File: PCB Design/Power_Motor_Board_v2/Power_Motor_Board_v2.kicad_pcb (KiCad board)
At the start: 2 copper layers, 98.2 x 100 mm, 38 parts, among them IC1 DRV8251ADDAR, IC3 DRV8251ADDAR, IC4 AP63205WU-7, J1 691137710002, J2 691137710002, J2A1 SSW-119-01-T-D, J3 691137710002, J4 Conn_01x06, J5 Conn_01x02_Socket

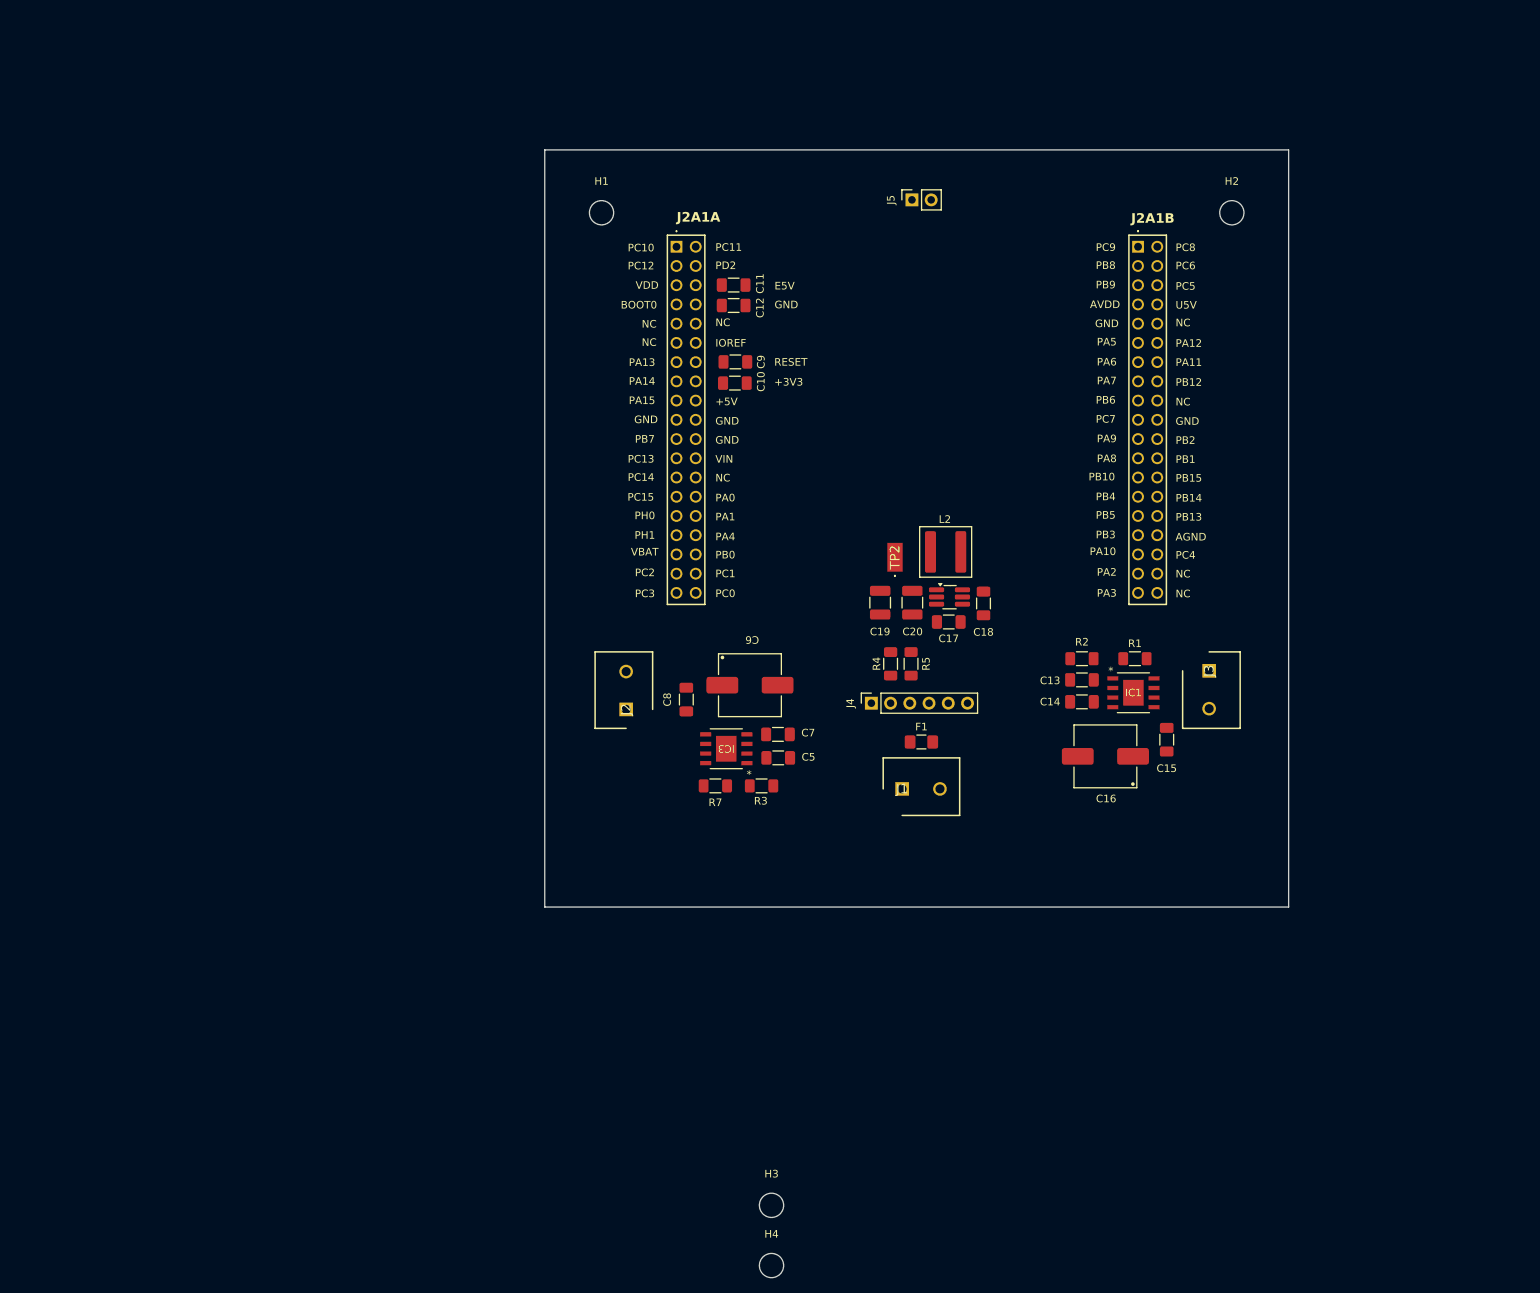
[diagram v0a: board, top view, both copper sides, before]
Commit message: Continued board layout and mesurements as well as edited BOM
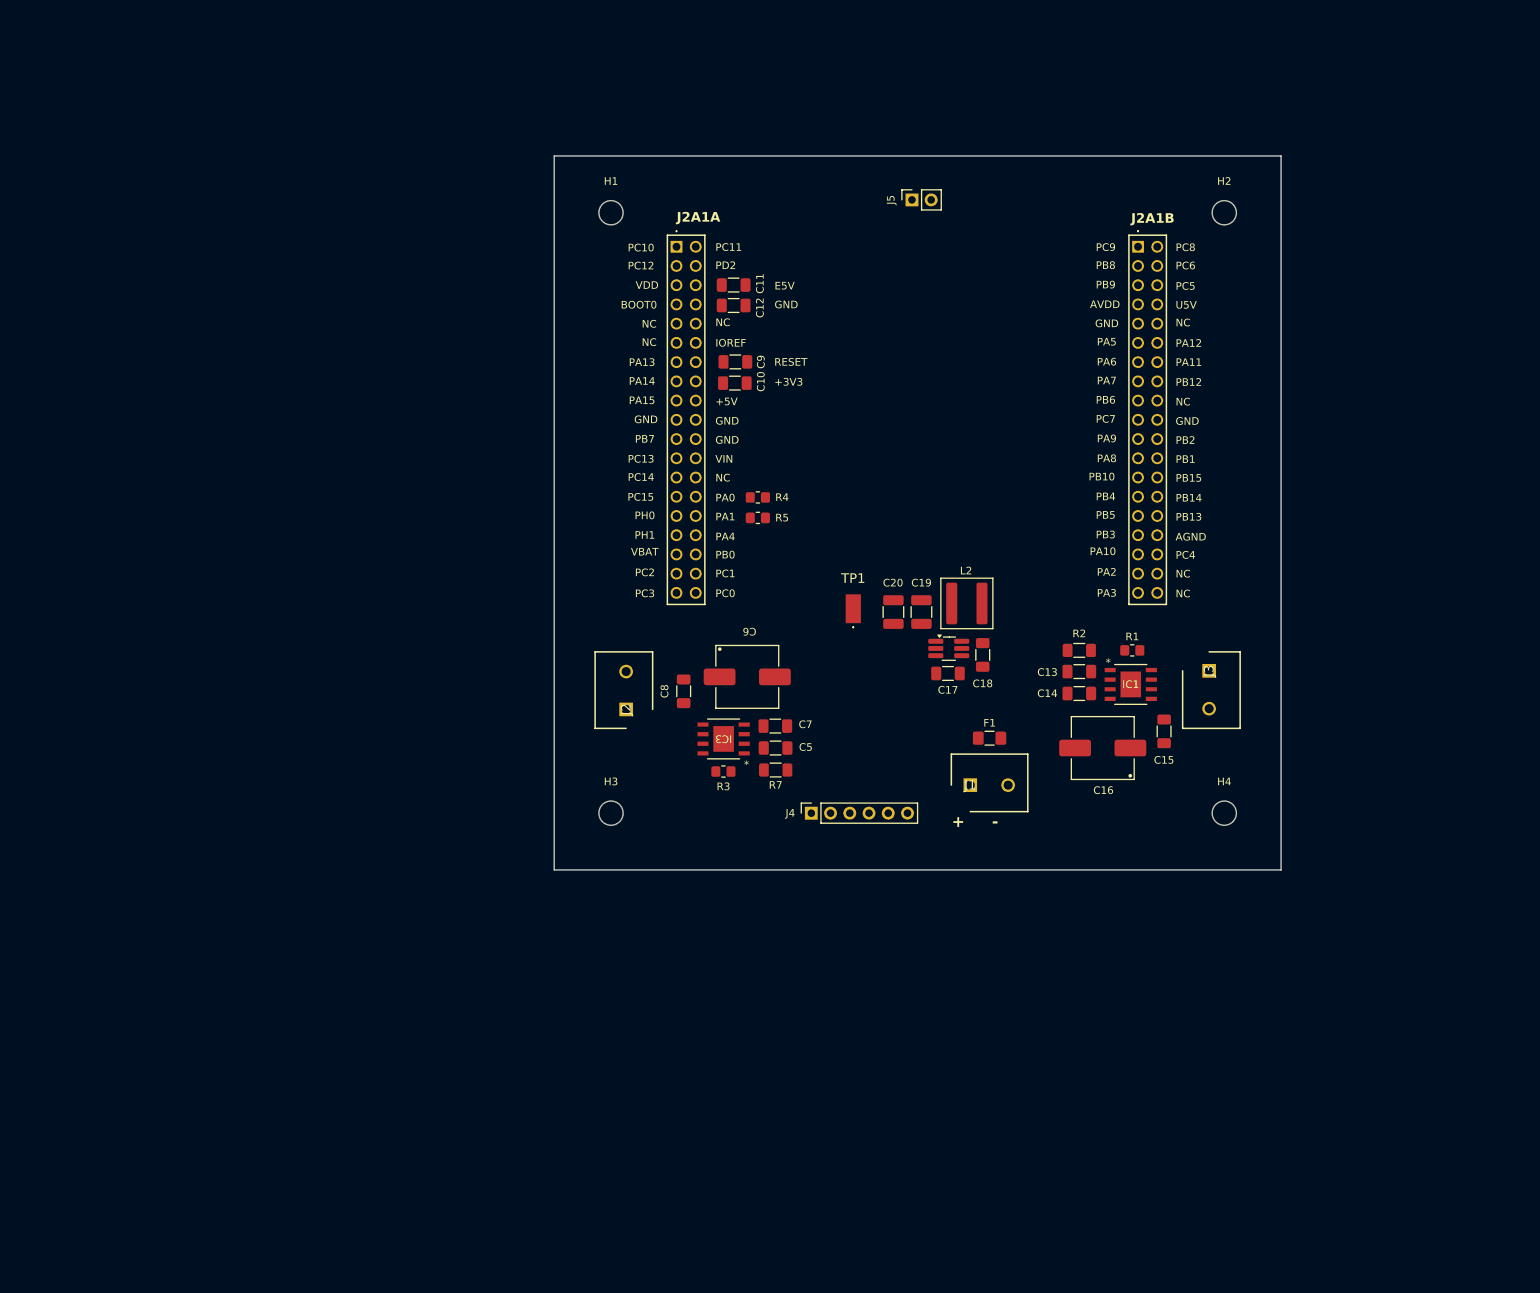
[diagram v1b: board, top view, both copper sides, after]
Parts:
- R1, R3, R4, R5: footprint Resistor_SMD:R_1206_3216Metric_Pad1.30x1.75mm_HandSolder -> Resistor_SMD:R_0805_2012Metric_Pad1.20x1.40mm_HandSolder
- moved H4 84.5 mm to (191.0, 126.0)
- moved H3 56.0 mm to (110.0, 126.0)
- moved R4 28.1 mm to (129.4, 84.3), turned to 0 degrees
- moved R5 27.9 mm to (129.4, 87.0), turned to 0 degrees
- moved J4 16.5 mm to (136.5, 126.0)
- moved F1 9.01 mm to (160.0, 116.1)
- moved J1 9.01 mm to (157.4, 122.3)
- moved TP1 8.75 mm to (142.0, 99.0)
- moved R7 8.23 mm to (131.8, 120.3), turned to 0 degrees
- moved L2 7.35 mm to (157.0, 98.3)
- moved C17 6.80 mm to (154.5, 107.5)
- moved C18 6.80 mm to (159.1, 105.1)
- moved IC4 6.80 mm to (154.6, 104.2)
- moved C19 5.59 mm to (151.0, 99.4), turned to -90 degrees
- moved R3 5.38 mm to (124.8, 120.5), turned to 0 degrees
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- renumbered TP2 to TP1
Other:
- board size 98.2 x 100 mm -> 96 x 94.3 mm
- board text added: "+ -"

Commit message: traced out the layout
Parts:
- R1, R3, R4, R5: footprint Resistor_SMD:R_0805_2012Metric_Pad1.20x1.40mm_HandSolder -> Resistor_SMD:R_1206_3216Metric_Pad1.30x1.75mm_HandSolder
- moved J2 77.2 mm to (189.0, 107.2), turned to -90 degrees
- moved J3 76.0 mm to (113.2, 112.3), turned to 90 degrees
- moved C15 63.7 mm to (119.8, 108.4), turned to 90 degrees
- moved C8 63.6 mm to (183.1, 113.9), turned to -90 degrees
- moved C16 59.7 mm to (122.1, 106.2), turned to 0 degrees
- moved C6 58.7 mm to (180.4, 115.8), turned to 180 degrees
- moved R1 56.8 mm to (124.0, 119.1), turned to 0 degrees
- moved R3 55.8 mm to (177.8, 103.0), turned to 180 degrees
- moved IC1 54.8 mm to (124.2, 114.6), turned to 180 degrees
- moved IC3 53.6 mm to (177.8, 107.6), turned to 0 degrees
- moved R2 43.4 mm to (130.9, 119.1), turned to 0 degrees
- moved R7 42.6 mm to (170.9, 103.5), turned to 180 degrees
- moved C13 41.9 mm to (130.9, 116.3), turned to 0 degrees
- moved C14 41.0 mm to (130.9, 113.4), turned to 0 degrees
- moved C5 40.7 mm to (170.9, 106.4), turned to 180 degrees
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- renumbered TP1 to TP2
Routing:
- net 5V_out: track 0.00 -> 134.8 mm
- net +3V3: track 0.00 -> 131.3 mm, vias 0 -> 4
- net /I_MTR2: track 0.00 -> 104.3 mm, vias 0 -> 1
- net +Vbatt: track 0.00 -> 83.0 mm
- net +5V: track 0.00 -> 80.9 mm
- net /IN1_MTR1: track 0.00 -> 69.2 mm, vias 0 -> 1
- net /IN2-MTR1: track 0.00 -> 68.9 mm, vias 0 -> 1
- net /IN2_MTR2: track 0.00 -> 51.6 mm
- net Net-(J4-Pin_2): track 0.00 -> 47.1 mm, vias 0 -> 2
- net Net-(J4-Pin_3): track 0.00 -> 43.4 mm, vias 0 -> 1
- net GND: track 0.00 -> 37.3 mm, vias 0 -> 20
- net /I_MTR1: track 0.00 -> 36.4 mm
- net /IN1_MTR2: track 0.00 -> 20.5 mm, vias 0 -> 1
- net Net-(IC4-SW): track 0.00 -> 13.1 mm
- net /+OUT_1: track 0.00 -> 11.0 mm
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- added copper zone on B.Cu, net GND
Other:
- board size 96 x 94.3 mm -> 95 x 92.8 mm

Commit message: changed to v2 main board
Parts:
- added G***: LOGO, LOGO, F.Cu at (150.7, 57.7)
- moved TP2 37.7 mm to (134.6, 63.1)
- moved C20 2.87 mm to (145.1, 105.0), turned to -90 degrees
- moved C19 2.54 mm to (148.8, 105.0), turned to -90 degrees
- moved L2 1.73 mm to (145.4, 98.0)
- moved C18 1.36 mm to (151.9, 100.4)
- moved J4 0.50 mm to (151.4, 121.8)
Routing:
- net +Vbatt: track 83.0 -> 94.2 mm
- net +5V: track 80.9 -> 77.2 mm
- net +3V3: track 131.3 -> 134.0 mm
- net GND: track 37.3 -> 35.9 mm
- net /I_MTR2: track 104.3 -> 103.1 mm
- net Net-(IC4-BST): track 2.88 -> 3.58 mm
- net Net-(J4-Pin_2): track 47.1 -> 47.6 mm
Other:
- board size 95 x 92.8 mm -> 93 x 90.8 mm
- board text added: "EN 5V GND RX TX ST"
- board text added: "GND 5V"
- board text added: "Team 37 UNOS"
- board text added: "amazingamy"
- board text added: "freddy fazbear"
- board text added: "jujuthepoopoo"
- board text added: "lean masheen"
- board text added: "whatdahaleeberry"

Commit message: fixed board, gerber bs, ummmmm and idk its also 1am and i have to wake at 6am ;-;
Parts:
- moved C17 4.37 mm to (157.0, 109.2)
- moved C18 4.37 mm to (153.2, 104.6)
- moved C19 4.37 mm to (150.0, 109.2)
- moved C20 4.37 mm to (146.3, 109.2)
- moved F1 4.37 mm to (161.2, 118.3)
- moved IC4 4.37 mm to (153.7, 109.1)
- moved J1 4.37 mm to (158.7, 124.5)
- moved L2 4.37 mm to (146.7, 102.2)
- moved J4 1.50 mm to (151.5, 120.3)
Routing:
- net +5V: track 77.2 -> 81.9 mm
- net 5V_out: track 135.1 -> 139.5 mm
- net +3V3: track 134.0 -> 137.2 mm
- net /I_MTR2: track 103.1 -> 100.4 mm
- net GND: track 35.9 -> 38.6 mm, vias 20 -> 104
- net Net-(J4-Pin_3): track 43.4 -> 41.4 mm
- net Net-(J4-Pin_2): track 47.6 -> 46.2 mm
- net +Vbatt: track 94.2 -> 95.4 mm
- net /-OUT_2: track 9.13 -> 9.70 mm
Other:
- board text added: "EN 5V GND TX RX ST"
- board text removed: "EN 5V GND RX TX ST"
